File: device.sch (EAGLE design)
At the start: 40 parts, among them CON1 B3B-ZR, CON2 B3B-ZR, CON3 B3B-ZR, CON4 B3B-ZR, CON5 B3B-ZR, J1 S2B-PH-SM4-TB(LF)(SN), Q1 2SC2712-GR(F), Q2 2SC2712-GR(F), Q3 2SC2712-GR(F), Q4 2SC2712-GR(F)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

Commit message: exchange VCC and GND
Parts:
- SV1: value (none) -> serial
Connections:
- net GND: now also J1.2; no longer J1.1
- net VIN: now also J1.1; no longer J1.2
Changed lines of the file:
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@@
 <part name="S2" library="SKRPACE010" deviceset="SKRPACE010" device=""/>
 <part name="C6" library="rcl" library_urn="urn:adsk.eagle:library:334" deviceset="C-EU" device="C0402" package3d_urn="urn:adsk.eagle:package:23626/2" value="0.1u"/>
-<part name="SV1" library="con-lstb" library_urn="urn:adsk.eagle:library:162" deviceset="MA03-1" device="" package3d_urn="urn:adsk.eagle:package:8339/1"/>
+<part name="SV1" library="con-lstb" library_urn="urn:adsk.eagle:library:162" deviceset="MA03-1" device="" package3d_urn="urn:adsk.eagle:package:8339/1" value="serial"/>
 <part name="R17" library="rcl" library_urn="urn:adsk.eagle:library:334" deviceset="R-EU_" device="R0603" package3d_urn="urn:adsk.eagle:package:23555/3" value="1k"/>
 <part name="GND6" library="supply1" library_urn="urn:adsk.eagle:library:371" deviceset="GND" device=""/>
@@
 </segment>
 <segment>
-<wire x1="73.66" y1="33.02" x2="99.06" y2="33.02" width="0.1524" layer="91"/>
-<label x="93.98" y="35.56" size="1.778" layer="95"/>
-<wire x1="99.06" y1="33.02" x2="109.22" y2="33.02" width="0.1524" layer="91"/>
-<wire x1="73.66" y1="33.02" x2="73.66" y2="22.86" width="0.1524" layer="91"/>
+<wire x1="73.66" y1="30.48" x2="99.06" y2="30.48" width="0.1524" layer="91"/>
+<label x="91.44" y="25.4" size="1.778" layer="95"/>
+<wire x1="73.66" y1="30.48" x2="73.66" y2="22.86" width="0.1524" layer="91"/>
 <pinref part="GND10" gate="1" pin="GND"/>
-<pinref part="J1" gate="G$1" pin="1"/>
-<junction x="99.06" y="33.02"/>
 <pinref part="J1" gate="G$1" pin="SHIELD"/>
-<wire x1="99.06" y1="33.02" x2="99.06" y2="25.4" width="0.1524" layer="91"/>
+<wire x1="99.06" y1="30.48" x2="99.06" y2="25.4" width="0.1524" layer="91"/>
 <wire x1="99.06" y1="25.4" x2="109.22" y2="25.4" width="0.1524" layer="91"/>
+<junction x="99.06" y="30.48"/>
+<pinref part="J1" gate="G$1" pin="2"/>
+<wire x1="99.06" y1="30.48" x2="109.22" y2="30.48" width="0.1524" layer="91"/>
 </segment>
 <segment>
@@
 <wire x1="60.96" y1="83.82" x2="60.96" y2="81.28" width="0.1524" layer="91"/>
 <wire x1="60.96" y1="83.82" x2="53.34" y2="83.82" width="0.1524" layer="91"/>
-<wire x1="53.34" y1="83.82" x2="53.34" y2="30.48" width="0.1524" layer="91"/>
-<label x="93.98" y="27.94" size="1.778" layer="95"/>
-<wire x1="53.34" y1="30.48" x2="109.22" y2="30.48" width="0.1524" layer="91"/>
-<pinref part="J1" gate="G$1" pin="2"/>
-</segment>
-<segment>
+<wire x1="53.34" y1="83.82" x2="53.34" y2="33.02" width="0.1524" layer="91"/>
+<label x="101.6" y="35.56" size="1.778" layer="95"/>
+<pinref part="J1" gate="G$1" pin="1"/>
+<wire x1="109.22" y1="33.02" x2="53.34" y2="33.02" width="0.1524" layer="91"/>
+</segment>
+<segment>

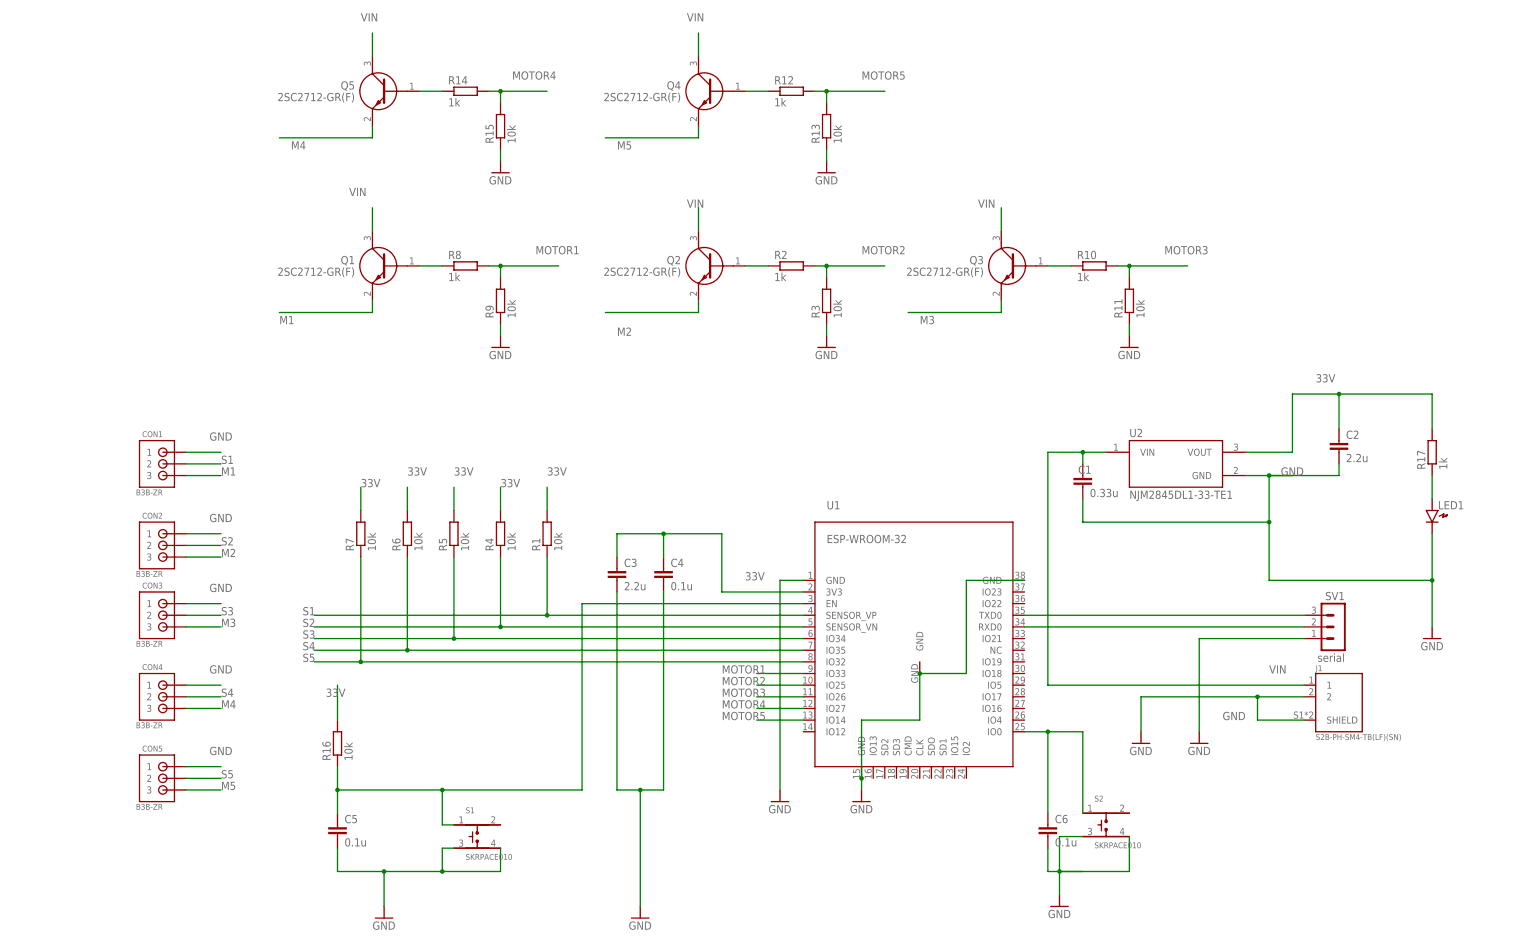
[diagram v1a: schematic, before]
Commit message: Manual routing of V2.0.0
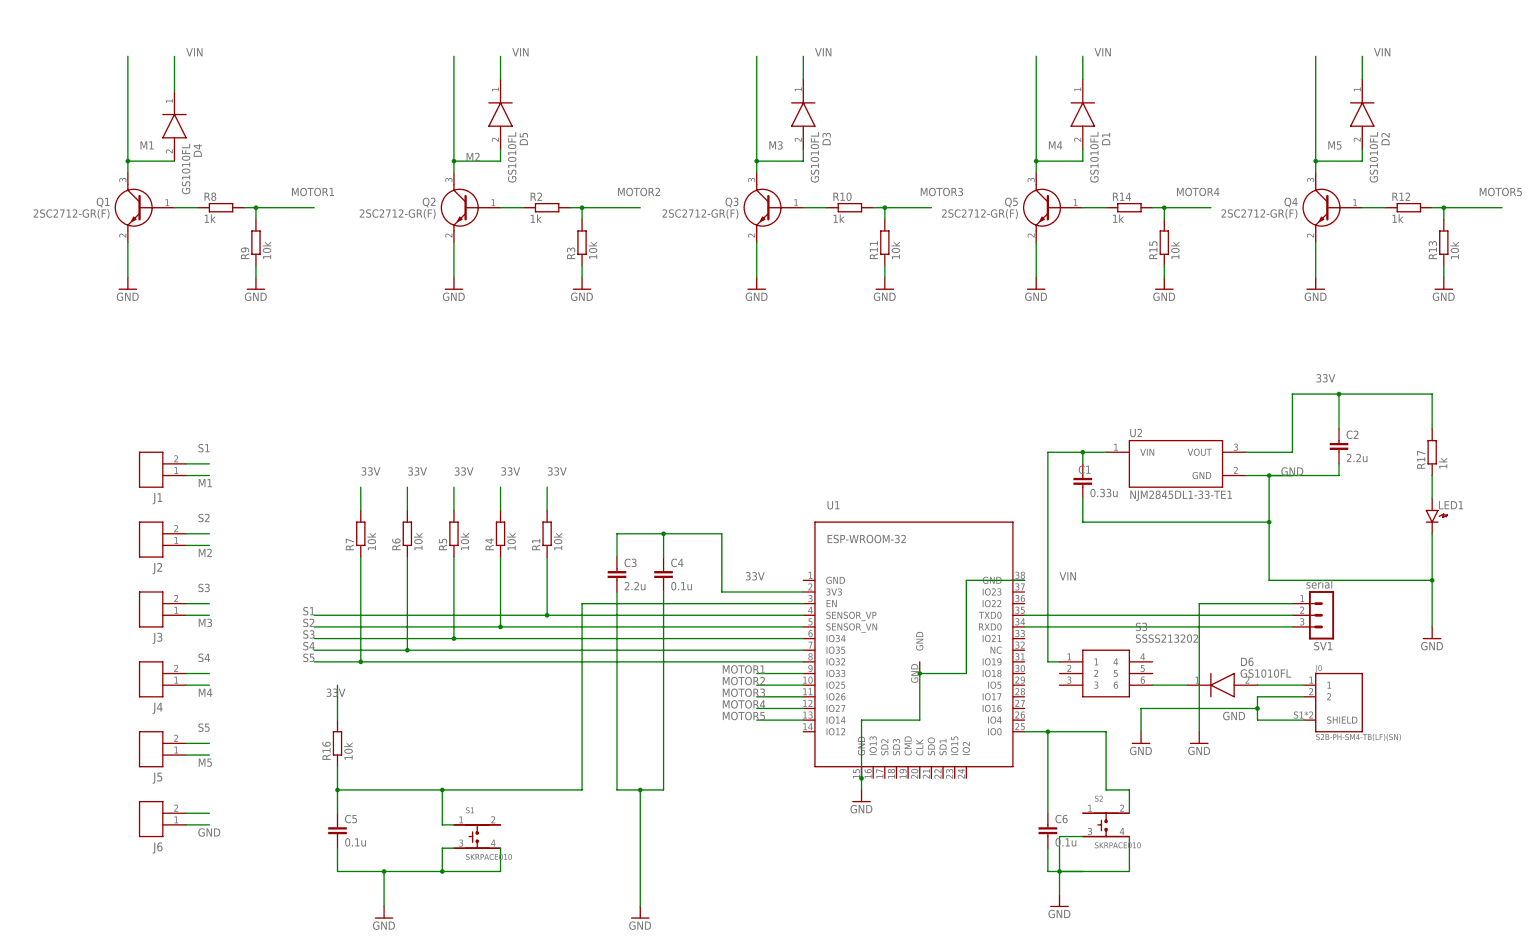
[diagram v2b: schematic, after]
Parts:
- removed CON1, CON2, CON3, CON4, CON5: B3B-ZR, jst:B3B-ZR
- added D1, D2, D3, D4, D5, D6: GS1010FL, GS1010FL:GS1010FL
- added J0: S2B-PH-SM4-TB(LF)(SN), S2B-PH-SM4-TB_LF__SN_:S2B-PH-SM4-TB(LF)(SN)
- added J2, J3, J4, J5, J6: JST_ZH_2PIN, kanflo:JST_ZH_2PIN
- added S3: SSSS213202, SSSS213202:SSSS213202
- J1: value S2B-PH-SM4-TB(LF)(SN) -> JST_ZH_2PIN; device S2B-PH-SM4-TB_LF__SN_:S2B-PH-SM4-TB(LF)(SN) -> kanflo:JST_ZH_2PIN
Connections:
- new net N$12: D6.A, J0.1
- new net N$8: D6.K, S3.6
- net GND: now also J0.2, J0.SHIELD, J6.P$1, Q1.E, Q2.E, Q3.E, Q4.E, Q5.E; no longer CON1.1, CON2.1, CON3.1, CON4.1, CON5.1, J1.2, J1.SHIELD, U1.GND@1
- net M1: now also D4.A, J1.P$1, Q1.C; no longer CON1.3, Q1.E
- net M2: now also D5.A, J2.P$1, Q2.C; no longer CON2.3, Q2.E
- net M3: now also D3.A, J3.P$1, Q3.C; no longer CON3.3, Q3.E
- net M4: now also D1.A, J4.P$1, Q5.C; no longer CON4.3, Q5.E
- net M5: now also D2.A, J5.P$1, Q4.C; no longer CON5.3, Q4.E
- net N$3: now also S2.2; no longer S2.1
- net N$4: now also SV1.2; no longer SV1.3
- net N$5: now also SV1.3; no longer SV1.2
- net S1: now also J1.P$2; no longer CON1.2
- net S2: now also J2.P$2; no longer CON2.2
- net S3: now also J3.P$2; no longer CON3.2
- net S4: now also J4.P$2; no longer CON4.2
- net S5: now also J5.P$2; no longer CON5.2
- net VIN: now also D1.K, D2.K, D3.K, D4.K, D5.K, J6.P$2, S3.1; no longer J1.1, Q1.C, Q2.C, Q3.C, Q4.C, Q5.C
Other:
- moved on the sheet: Q1, Q2, Q3, Q4, Q5, R10, R11, R12, R13, R14, R15, R2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
